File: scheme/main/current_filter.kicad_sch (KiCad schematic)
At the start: 10 parts

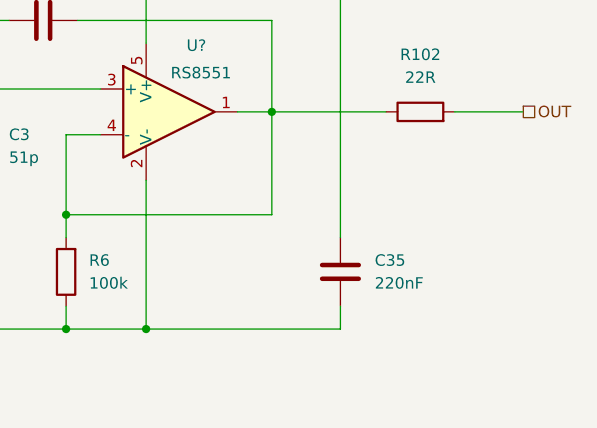
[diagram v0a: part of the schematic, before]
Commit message: replace some 220n capacitors with 100n
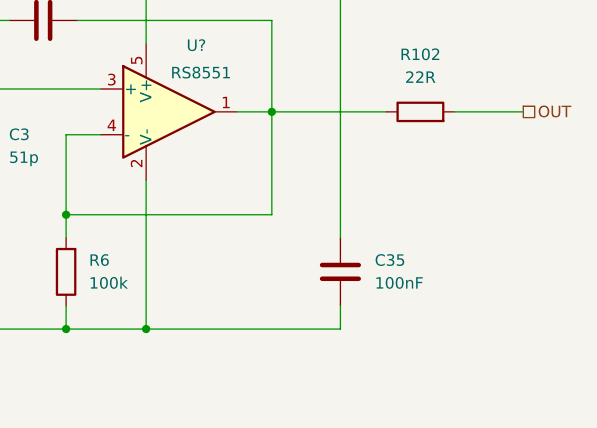
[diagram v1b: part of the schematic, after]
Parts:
- C35: value 220nF -> 100nF
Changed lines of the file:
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@@
 			)
 		)
-		(property "Value" "220nF"
+		(property "Value" "100nF"
 			(at 138.43 87.6299 0)
 			(effects

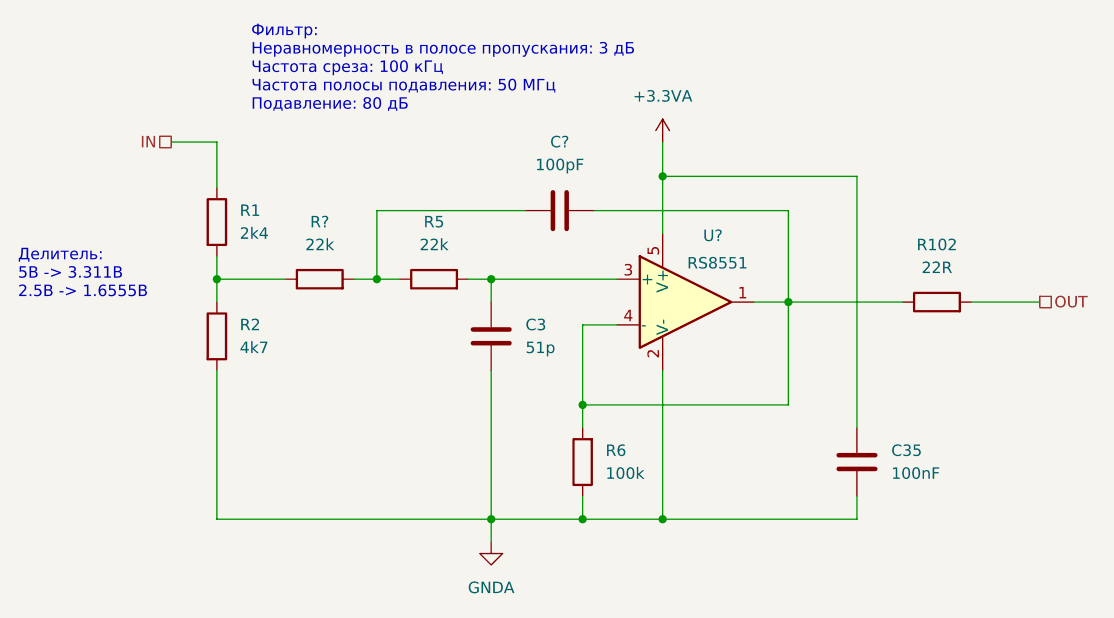
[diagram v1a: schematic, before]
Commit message: set names to unnamed components
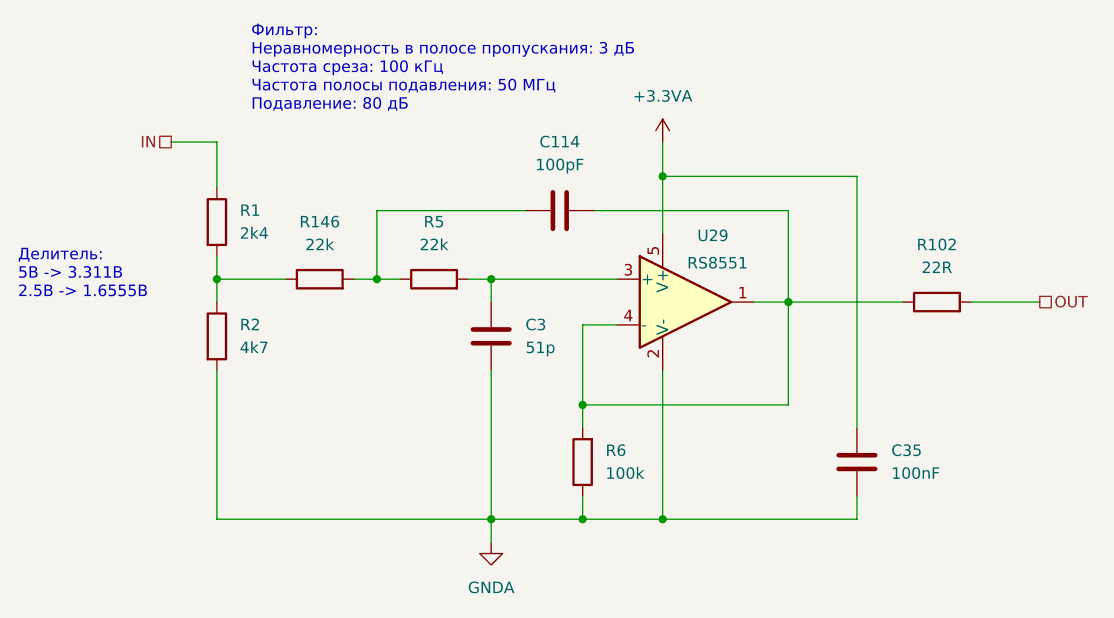
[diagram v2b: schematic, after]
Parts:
- gave numbers to parts that had none: 3
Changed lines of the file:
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@@
 		(dnp no)
 		(fields_autoplaced yes)
-		(property "Reference" "R?"
+		(property "Reference" "R146"
 			(at 74.93 59.69 90)
 			(effects
@@
 			(project "main"
 				(path "/c11d1dbc-4db9-4712-8d1d-5f6f7086cded/4b1be1b1-dfa5-4b57-a4fe-e097b3b33d8a"
-					(reference "R?")
+					(reference "R146")
 					(unit 1)
 				)
@@
 		(on_board yes)
 		(dnp no)
-		(property "Reference" "U?"
+		(property "Reference" "U29"
 			(at 118.618 61.214 0)
 			(effects
@@
 			(project "main"
 				(path "/c11d1dbc-4db9-4712-8d1d-5f6f7086cded/4b1be1b1-dfa5-4b57-a4fe-e097b3b33d8a"
-					(reference "U?")
+					(reference "U29")
 					(unit 1)
 				)
@@
 		(dnp no)
 		(fields_autoplaced yes)
-		(property "Reference" "C?"
+		(property "Reference" "C114"
 			(at 101.6 50.8 90)
 			(effects
@@
 			(project "main"
 				(path "/c11d1dbc-4db9-4712-8d1d-5f6f7086cded/4b1be1b1-dfa5-4b57-a4fe-e097b3b33d8a"
-					(reference "C?")
+					(reference "C114")
 					(unit 1)
 				)
@@
 		(dnp no)
 		(fields_autoplaced yes)
-		(property "Reference" "#PWR?"
+		(property "Reference" "#PWR149"
 			(at 113.03 54.61 0)
 			(effects
@@
 			(project "main"
 				(path "/c11d1dbc-4db9-4712-8d1d-5f6f7086cded/4b1be1b1-dfa5-4b57-a4fe-e097b3b33d8a"
-					(reference "#PWR?")
+					(reference "#PWR149")
 					(unit 1)
 				)
@@
 		(dnp no)
 		(fields_autoplaced yes)
-		(property "Reference" "#PWR?"
+		(property "Reference" "#PWR148"
 			(at 93.98 101.6 0)
 			(effects
@@
 			(project "main"
 				(path "/c11d1dbc-4db9-4712-8d1d-5f6f7086cded/4b1be1b1-dfa5-4b57-a4fe-e097b3b33d8a"
-					(reference "#PWR?")
-					(unit 1)
-				)
+					(reference "#PWR148")
+					(unit 1)
+				)

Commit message: sheets titles
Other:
- title: (none) -> Фильтр тока
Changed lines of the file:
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@@
 	(generator_version "8.0")
 	(paper "A4")
+	(title_block
+		(title "Фильтр тока")
+	)
 	(junction
 		(at 127 68.58)
